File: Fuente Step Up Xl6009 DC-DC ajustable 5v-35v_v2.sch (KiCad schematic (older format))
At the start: 16 parts, among them J1 Screw_Terminal_01x02, J2 Screw_Terminal_01x02, U1 XL6009E1

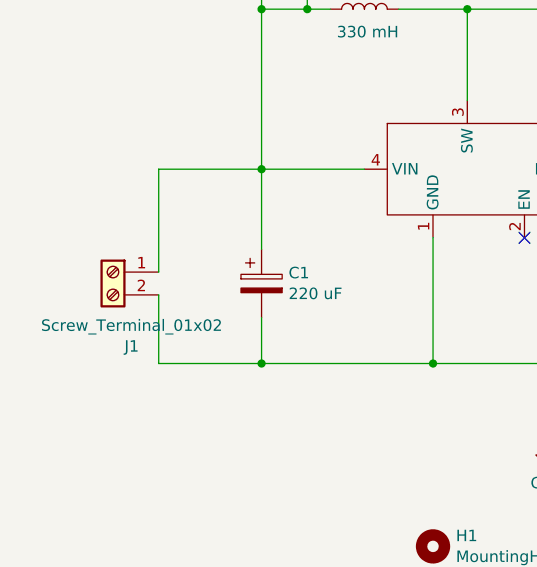
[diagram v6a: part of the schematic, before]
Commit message: Se acomodaron componentes y acortaron rutas
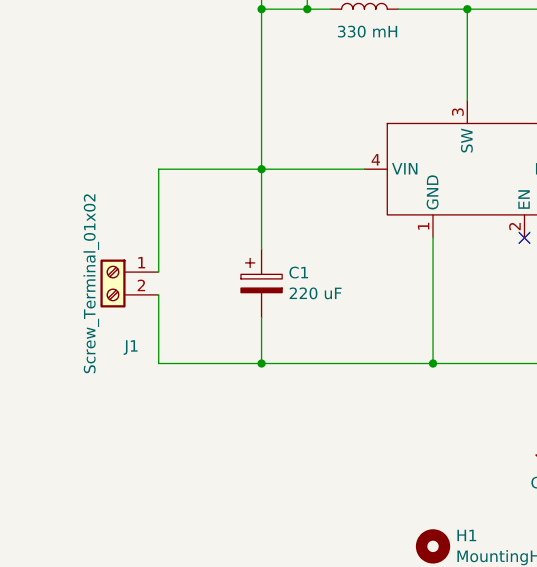
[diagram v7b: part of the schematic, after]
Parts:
- J1, J2: Field5 (none) -> OSTTA024163; Field7 (none) -> https://www.digikey.com/product-detail/en/on-shore-technolo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
- L1: Field5 (none) -> DR1050-330-R; Field7 (none) -> https://www.digikey.com/product-detail/en/eaton-electronics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
- R1: Field5 3296W-103-ND -> Y16361K00000T9W; Field7 https://www.digikey.com/product-detail/en/bourns-inc/3296W-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 -> https://www.digikey.com/product-detail/en/vishay-foil-resis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
- RV1: Field5 (none) -> 3296W-103-ND; Field7 (none) -> https://www.digikey.com/product-detail/en/bourns-inc/3296W-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
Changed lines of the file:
@@
 F 2 "Potentiometer_THT:Potentiometer_Bourns_3296W_Vertical" H 6600 3050 50  0001 C CNN
 F 3 "~" H 6600 3050 50  0001 C CNN
+F 4 "3296W-103-ND" H 6600 3050 50  0001 C CNN "Field5"
+F 5 "https://www.digikey.com/product-detail/en/bourns-inc/3296W-1-103/3296W-103-ND/84523" H 6600 3050 50  0001 C CNN "Field7"
 	1    6600 3050
 	-1   0    0    1
@@
 F 2 "Resistor_SMD:R_1806_4516Metric" V 6530 3550 50  0001 C CNN
 F 3 "Resistor_SMD:R_0805_2012Metric_Pad1.15x1.40mm_HandSolder" H 6600 3550 50  0001 C CNN
-F 4 "3296W-103-ND" H 6600 3550 50  0001 C CNN "Field5"
-F 5 "https://www.digikey.com/product-detail/en/bourns-inc/3296W-1-103/3296W-103-ND/84523" H 6600 3550 50  0001 C CNN "Field7"
+F 4 "Y16361K00000T9W" H 6600 3550 50  0001 C CNN "Field5"
+F 5 "https://www.digikey.com/product-detail/en/vishay-foil-resistors-division-of-vishay-precision-group/Y16361K00000T9W/Y1636-1K-ND/2512039" H 6600 3550 50  0001 C CNN "Field7"
 	1    6600 3550
 	1    0    0    -1
@@
 F 2 "Inductor_SMD:L_12x12mm_H8mm" H 5000 2350 50  0001 C CNN
 F 3 "~" H 5000 2350 50  0001 C CNN
+F 4 "DR1050-330-R" H 5000 2350 50  0001 C CNN "Field5"
+F 5 "https://www.digikey.com/product-detail/en/eaton-electronics-division/DR1050-330-R/513-1418-1-ND/1555567" H 5000 2350 50  0001 C CNN "Field7"
 	1    5000 2350
 	0    -1   -1   0
@@
 P 3900 3500
 F 0 "J1" H 3818 3175 50  0000 C CNN
-F 1 "Screw_Terminal_01x02" H 3818 3266 50  0000 C CNN
+F 1 "Screw_Terminal_01x02" V 4000 3450 50  0000 C CNN
 F 2 "TerminalBlock:TerminalBlock_Altech_AK300-2_P5.00mm" H 3900 3500 50  0001 C CNN
 F 3 "~" H 3900 3500 50  0001 C CNN
+F 4 "OSTTA024163" H 3900 3500 50  0001 C CNN "Field5"
+F 5 "https://www.digikey.com/product-detail/en/on-shore-technology-inc/OSTTA024163/ED2580-ND/614529" H 3900 3500 50  0001 C CNN "Field7"
 	1    3900 3500
 	-1   0    0    -1
@@
 F 2 "TerminalBlock:TerminalBlock_Altech_AK300-2_P5.00mm" H 7800 3000 50  0001 C CNN
 F 3 "~" H 7800 3000 50  0001 C CNN
+F 4 "OSTTA024163" H 7800 3000 50  0001 C CNN "Field5"
+F 5 "https://www.digikey.com/product-detail/en/on-shore-technology-inc/OSTTA024163/ED2580-ND/614529" H 7800 3000 50  0001 C CNN "Field7"
 	1    7800 3000
 	1    0    0    -1
